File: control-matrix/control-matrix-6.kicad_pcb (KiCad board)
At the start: 2 copper layers, 120 x 30 mm, 23 parts, among them J1 Screw_Terminal_01x02, J2 Screw_Terminal_01x02, J3 Screw_Terminal_01x02, J4 Screw_Terminal_01x02, J5 Screw_Terminal_01x02, J6 Screw_Terminal_01x02, J9 Screw_Terminal_01x02, SW1 SW_Rotary_1x12

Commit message: control-matrix: add power input labels on silkscreen
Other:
- board text added: "GND +12V"
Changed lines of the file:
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@@
 		(layer "Edge.Cuts")
+	)
+	(gr_text "GND  +12V"
+		(at 170.4 81.6 0)
+		(layer "F.SilkS")
+		(effects
+			(font
+				(size 1 1)
+				(thickness 0.2)
+				(bold yes)
+			)
+			(justify left bottom)
+		)
 	)
 	(segment

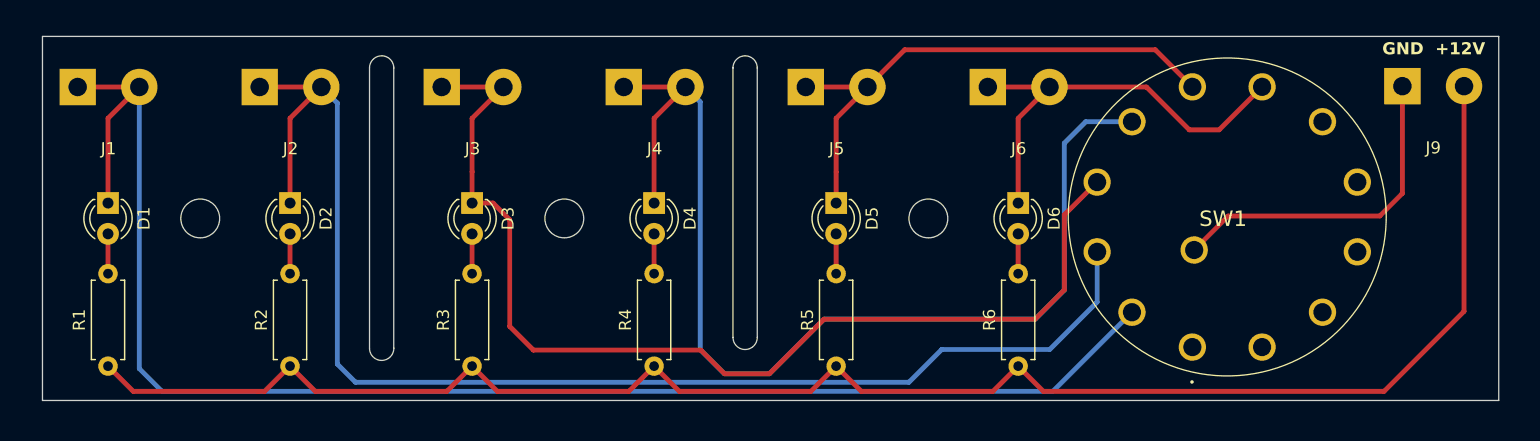
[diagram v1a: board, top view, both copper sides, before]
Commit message: control-matrix: add ground planes
This avoids having to etch too much copper.
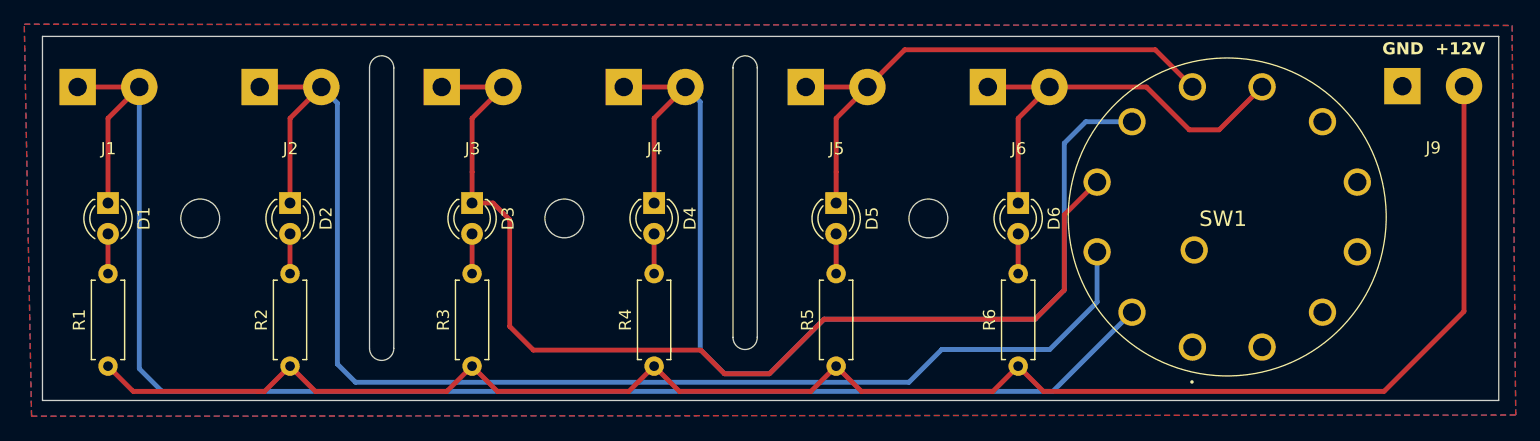
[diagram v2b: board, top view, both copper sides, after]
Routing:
- net GND: track 27.9 -> 0.00 mm
- added copper zone on B.Cu, net GND
- added copper zone on F.Cu, net GND
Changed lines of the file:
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@@
-	)
-	(segment
-		(start 172.06 92.94)
-		(end 170.2 94.8)
-		(width 0.4)
-		(layer "F.Cu")
-		(net 15)
-	)
-	(segment
-		(start 172.06 84.1)
-		(end 172.06 92.94)
-		(width 0.4)
-		(layer "F.Cu")
-		(net 15)
-	)
-	(segment
-		(start 170.2 94.8)
-		(end 157.70533 94.8)
-		(width 0.4)
-		(layer "F.Cu")
-		(net 15)
-	)
-	(segment
-		(start 157.70533 94.8)
-		(end 154.90475 97.60058)
-		(width 0.4)
-		(layer "F.Cu")
-		(net 15)
 	)
 	(segment
@@
 		(net 16)
 	)
+	(zone
+		(net 15)
+		(net_name "GND")
+		(layers "F.Cu" "B.Cu")
+		(hatch edge 0.5)
+		(connect_pads
+			(clearance 0.5)
+		)
+		(min_thickness 0.25)
+		(filled_areas_thickness no)
+		(fill yes
+			(thermal_gap 0.5)
+			(thermal_bridge_width 0.5)
+		)
+		(polygon
+			(pts
+				(xy 58.5 79) (xy 181.1 79.1) (xy 181.4 111.2) (xy 59.1 111.3)
+			)
+		)
+	)
 	(group ""
